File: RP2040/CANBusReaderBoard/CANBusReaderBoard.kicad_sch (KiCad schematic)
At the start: 13 parts, among them J0 RJ45, J1 RJ45, J2 RJ45, J3 RJ45, U1 MCP2515-xSO, U1 RP2040, Y1 Crystal

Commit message: Components all added, need to figure out RP2040 Powering and supplemental components.
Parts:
- removed U1: MCP2515-xSO, Package_SO:SOIC-18W_7.5x11.6mm_P1.27mm, symbol Interface_CAN_LIN:MCP2515-xSO
- removed Y1: Crystal, symbol Device:Crystal
- added C? (x2): 15 pF, Capacitor_THT:C_Axial_L3.8mm_D2.6mm_P7.50mm_Horizontal, symbol Device:C
- added CONTROLLER_1: MCP2515, MCP2515:MCP2515-E&slash_P, symbol Interface_CAN_LIN:MCP2515-xSO
- added J?: Terminate CAN, TerminalBlock_Phoenix:TerminalBlock_Phoenix_MKDS-3-2-5.08_1x02_P5.08mm_Horizontal, symbol Connector_Generic:Conn_01x02
- added R?: 120, Resistor_THT:R_Axial_DIN0204_L3.6mm_D1.6mm_P5.08mm_Horizontal, symbol Device:R_US
- added R?: 10K, Resistor_THT:R_Axial_DIN0204_L3.6mm_D1.6mm_P5.08mm_Horizontal, symbol Device:R_US
- added SW?: SW_DIP_x01, symbol Switch:SW_DIP_x01
- added TRANSCEIVER_1: MCP2562FD, MCP2562FD:MCP2562FD-H&slash_P, symbol MCP2562FD:MCP2562FD-H/P
- added Y?: Crystal 20Mhz, symbol Device:Crystal
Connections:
- net GND: now also C?.1, C?.1, CONTROLLER_1.9 (VSS), TRANSCEIVER_1.3 (VDD)
- net MISO: now also CONTROLLER_1.15 (SO)
- net MOSI: now also CONTROLLER_1.14 (SI)
- new net: R?.1, SW?.1
- new net: C?.2, CONTROLLER_1.8 (OSC1), Y?.1
- new net: C?.2, CONTROLLER_1.7 (OSC2), Y?.2
- new net: CONTROLLER_1.17 (~{RESET}), R?.1
- new net +3V3: CONTROLLER_1.18 (VDD), TRANSCEIVER_1.2 (VSS)
- new net CANH: J?.1 (Pin_1), SW?.2, TRANSCEIVER_1.7 (CANH)
- new net CANL: J?.2 (Pin_2), R?.2, TRANSCEIVER_1.6 (CANL)
- new net CS0: CONTROLLER_1.13 (SCK)
- new net RX: CONTROLLER_1.2 (RXCAN), TRANSCEIVER_1.4 (RXD)
- new net SPICLK: CONTROLLER_1.16 (~{CS})
- new net TX: CONTROLLER_1.1 (TXCAN), TRANSCEIVER_1.1 (TXD)

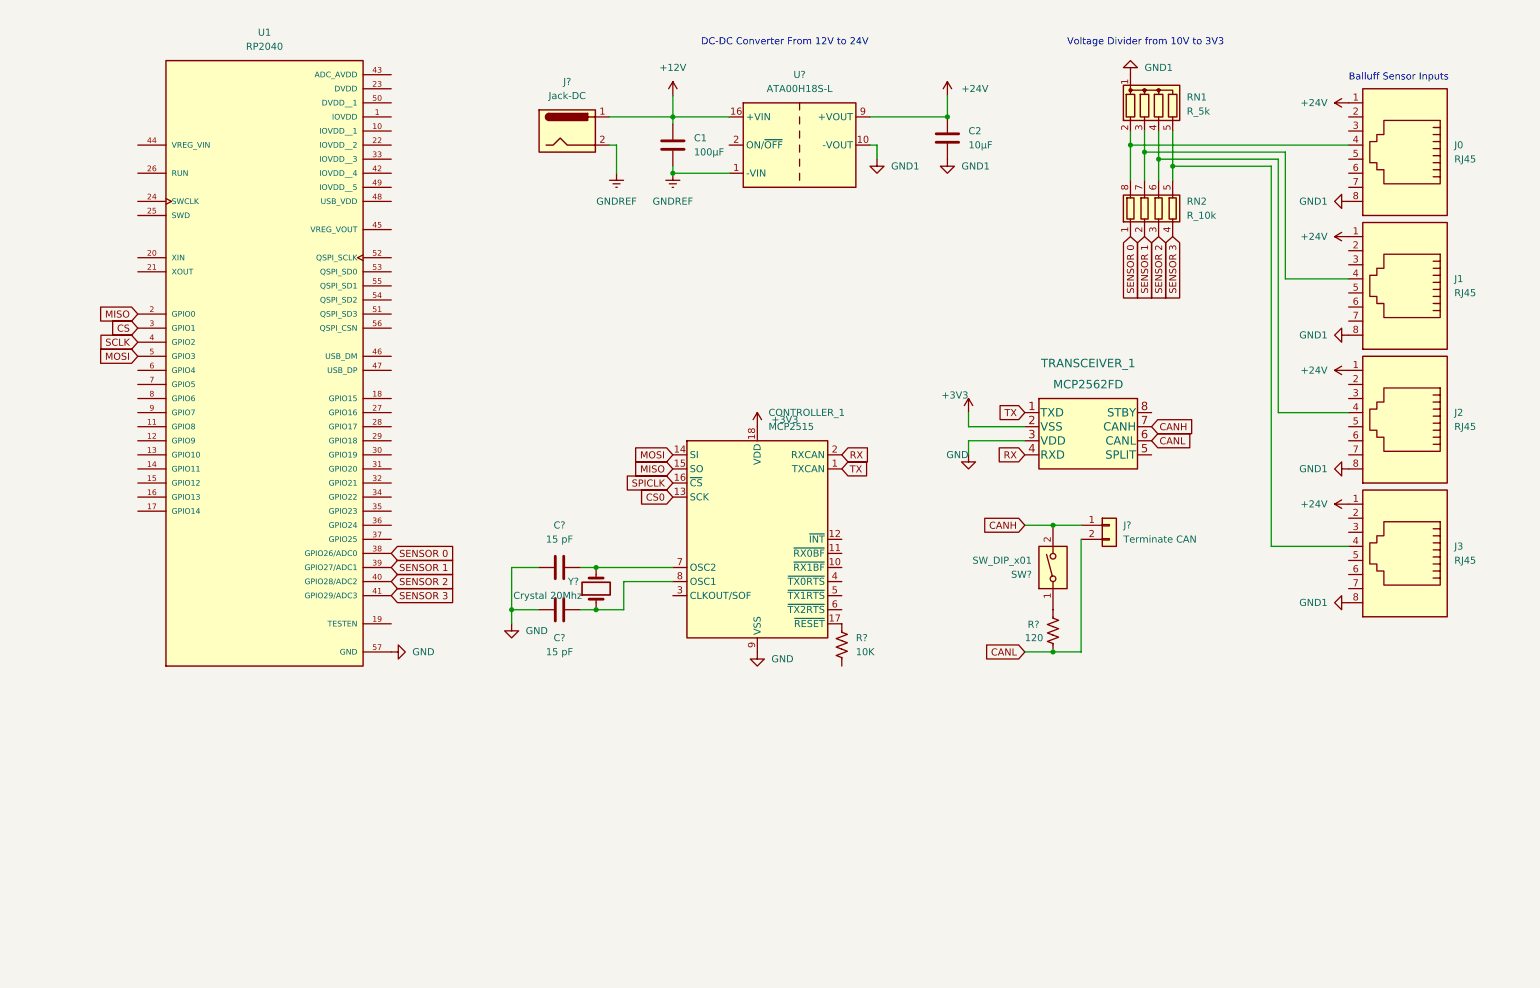
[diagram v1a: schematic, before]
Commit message: voltage regultor to 3.3v
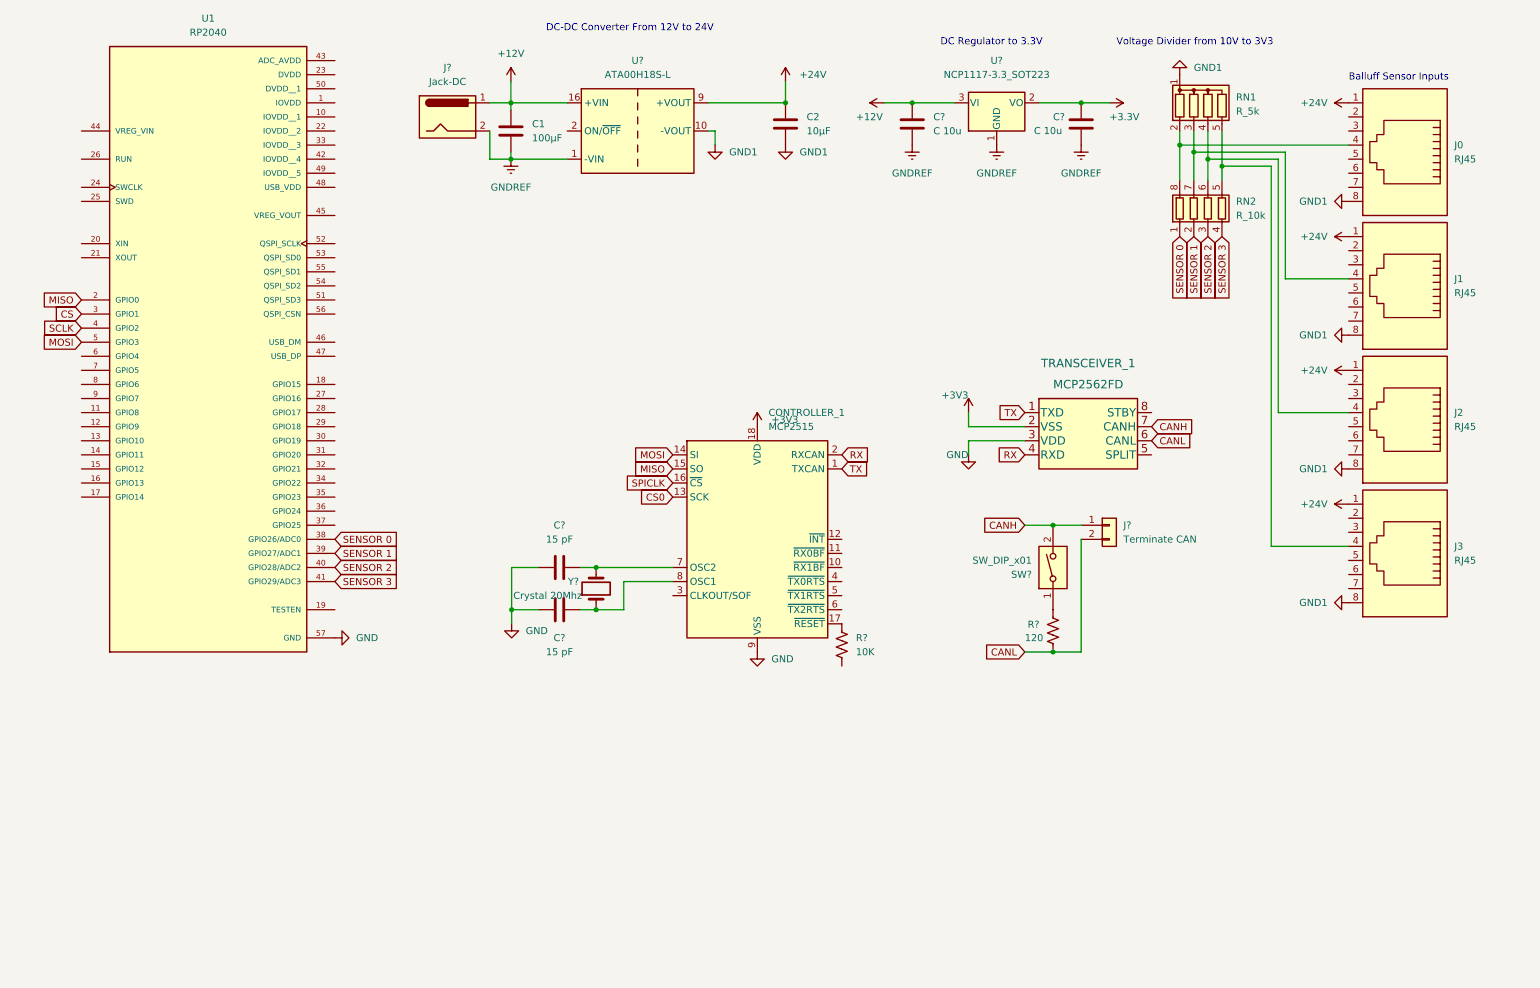
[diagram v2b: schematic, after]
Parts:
- added C? (x2): C 10u, symbol Device:C
- added U?: NCP1117-3.3_SOT223, Package_TO_SOT_SMD:SOT-223-3_TabPin2, symbol Regulator_Linear:NCP1117-3.3_SOT223
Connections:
- net +12V: now also C?.1, U?.3 (VI)
- net GNDREF: now also C?.2, C?.2, U?.1 (GND)
- new net +3.3V: C?.1, U?.2 (VO)
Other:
- note added: "DC Regulator to 3.3V"
- moved on the sheet: C1, C2, J?, RN1, RN2, U1, U?

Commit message: Working on status leds now
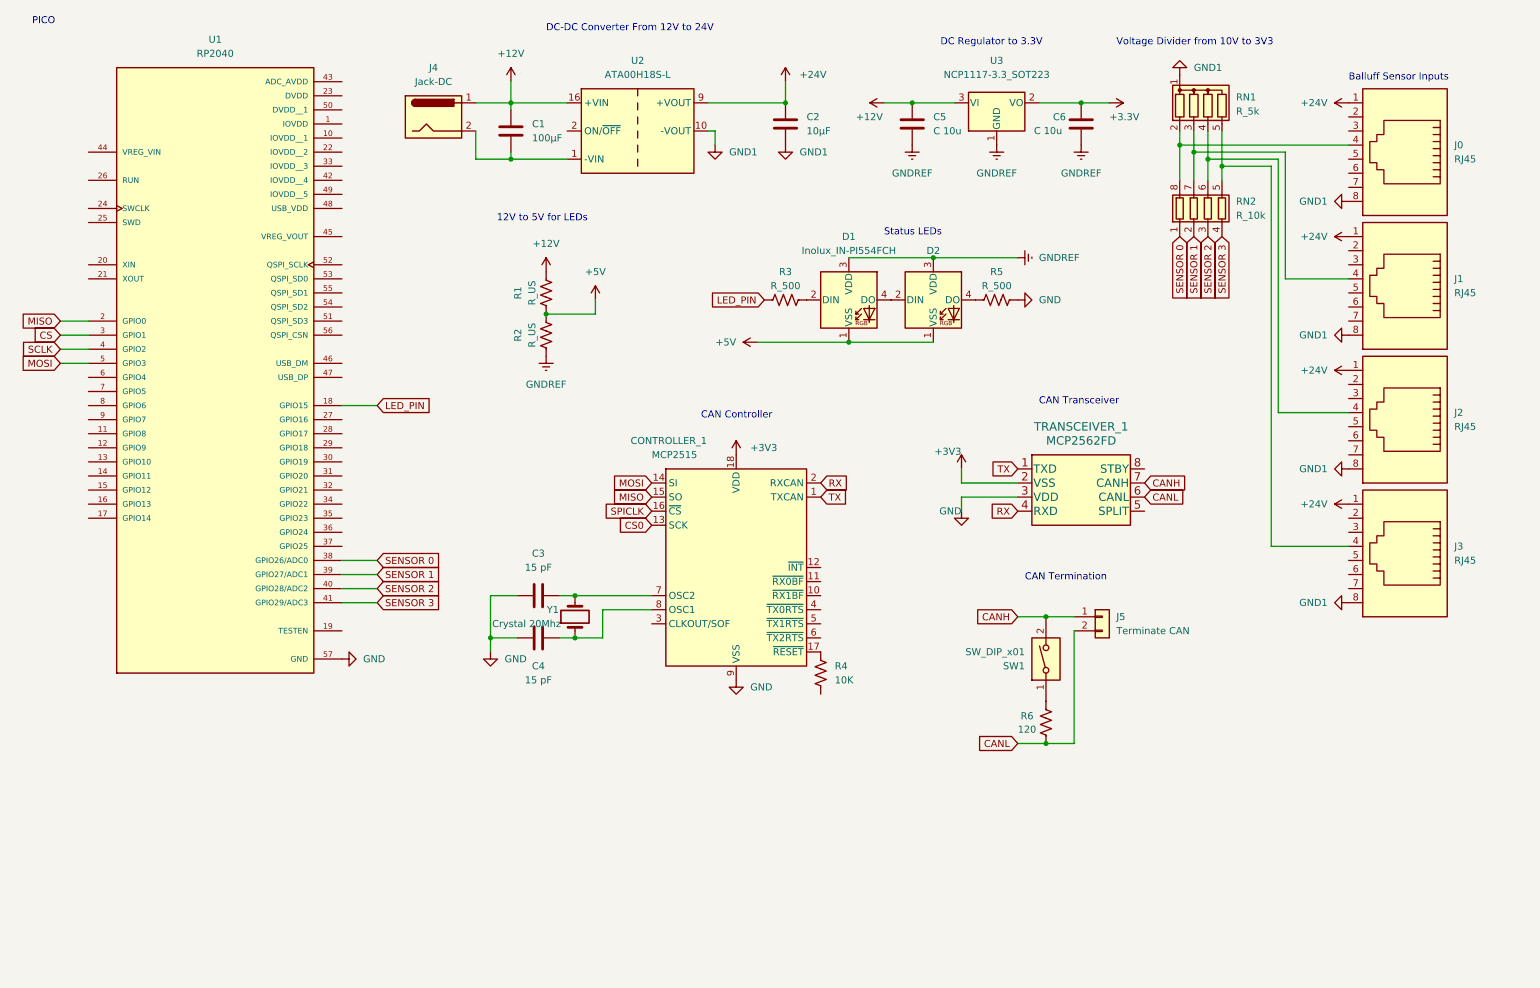
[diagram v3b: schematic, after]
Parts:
- added D1, D2: Inolux_IN-PI554FCH, LED_SMD:LED_Inolux_IN-PI554FCH_PLCC4_5.0x5.0mm_P3.2mm, symbol LED:Inolux_IN-PI554FCH
- added R1, R2: R_US, symbol Device:R_US
- added R3, R5: R_500, symbol Device:R_US
- gave numbers to parts that had none: 12
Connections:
- net +12V: now also R1.2
- net GND: now also R5.2
- net GNDREF: now also D1.3 (VDD), D2.3 (VDD), R2.1; no longer C1.2, J4.2, U2.1 (-VIN)
- net LED_PIN: now reaches U1.18 (GPIO15)
- net LED_PIN: now also R3.1
- new net: D1.4 (DO), D2.2 (DIN)
- new net: D2.4 (DO), R5.1
- new net: C1.2, J4.2, U2.1 (-VIN)
- new net: D1.2 (DIN), R3.2
- new net +5V: D1.1 (VSS), D2.1 (VSS), R1.1, R2.2
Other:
- note added: "12V to 5V for LEDs"
- note added: "CAN Controller"
- note added: "CAN Termination"
- note added: "CAN Transceiver"
- note added: "PICO"
- note added: "Status LEDs"
- moved on the sheet: C3, C4, CONTROLLER_1, J4, J5, R4, R6, SW1, TRANSCEIVER_1, U1, Y1

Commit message: cahnged to pico from rp2040
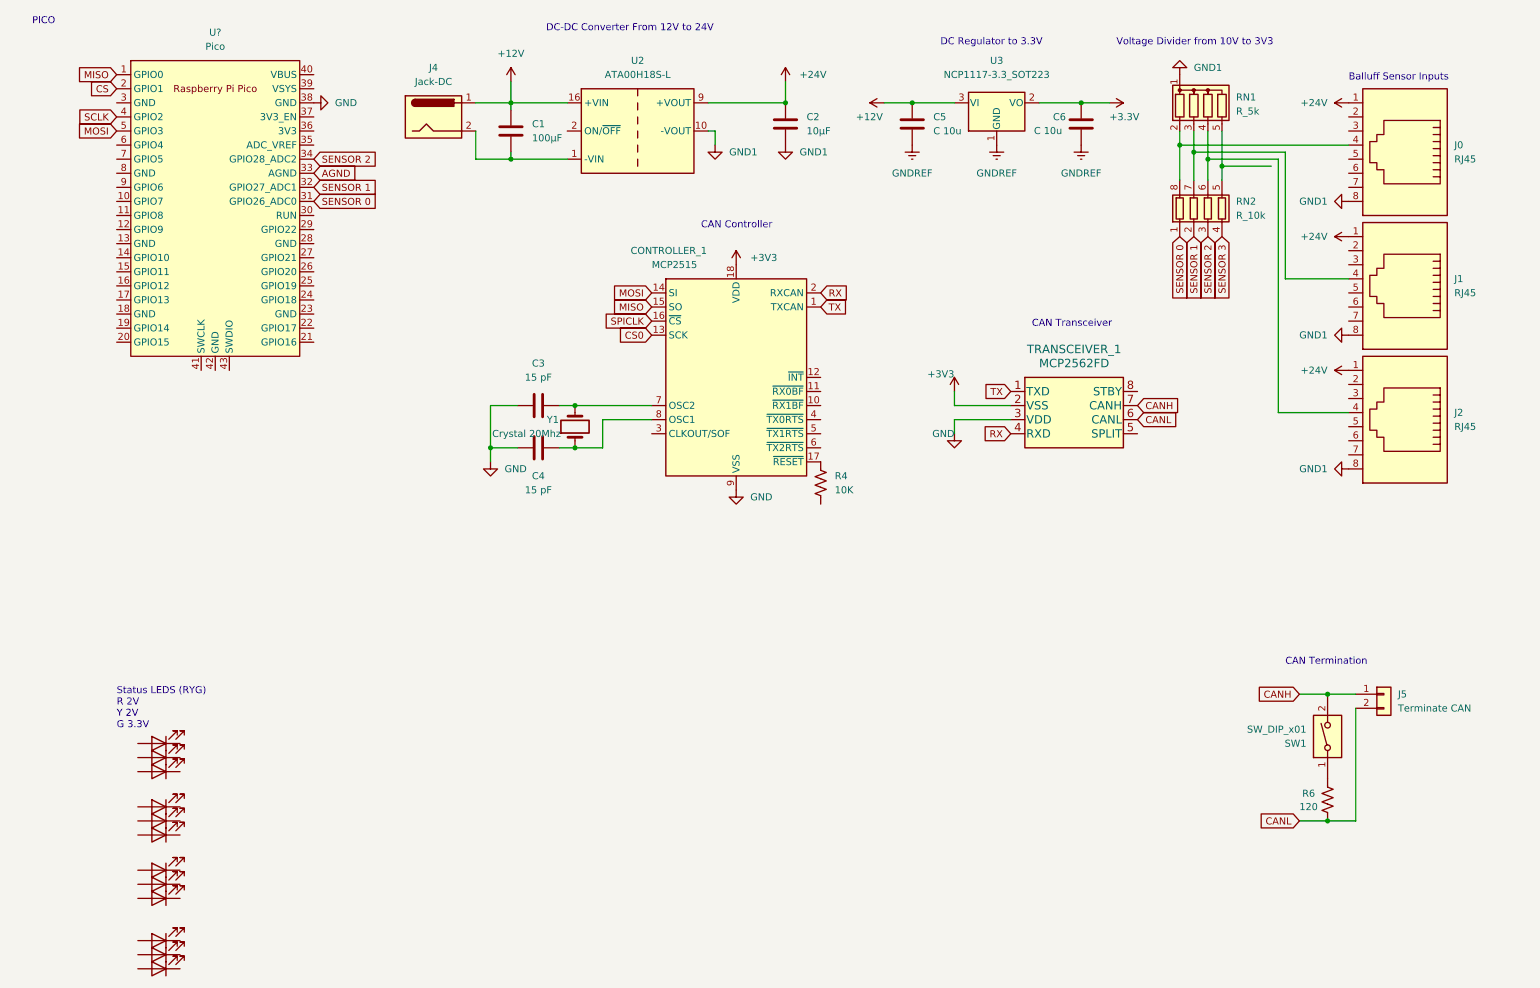
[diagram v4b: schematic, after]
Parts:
- removed D1, D2: Inolux_IN-PI554FCH, LED_SMD:LED_Inolux_IN-PI554FCH_PLCC4_5.0x5.0mm_P3.2mm, symbol LED:Inolux_IN-PI554FCH
- removed J3: RJ45, symbol Connector:RJ45
- removed R1, R2: R_US, symbol Device:R_US
- removed R3, R5: R_500, symbol Device:R_US
- removed U1: RP2040, RP2040:RP2040, symbol RP2040:RP2040
- added D? (x12): LED, symbol Device:LED
- added U?: Pico, RPi_Pico:RPi_Pico_SMD_TH, symbol MCU_RaspberryPi_and_Boards:Pico
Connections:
- net CS: now also U?.2 (GPIO1)
- net GND: now also U?.38 (GND)
- net MISO: now also U?.1 (GPIO0)
- net MOSI: now also U?.5 (GPIO3)
- net SCLK: now also U?.4 (GPIO2)
- net SENSOR 0: now also U?.31 (GPIO26_ADC0)
- net SENSOR 1: now also U?.32 (GPIO27_ADC1)
- net SENSOR 2: now also U?.34 (GPIO28_ADC2)
- new net AGND: U?.33 (AGND)
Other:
- note added: "Status LEDS (RYG) R 2V Y 2V G 3.3V"
- note removed: "12V to 5V for LEDs"
- note removed: "Status LEDs"
- moved on the sheet: C3, C4, CONTROLLER_1, J5, R4, R6, SW1, TRANSCEIVER_1, Y1

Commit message: .
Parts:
- removed CONTROLLER_1: MCP2515, MCP2515:MCP2515-E&slash_P, symbol Interface_CAN_LIN:MCP2515-xSO
- removed D? (x12): LED, symbol Device:LED
- removed R4: 10K, Resistor_THT:R_Axial_DIN0204_L3.6mm_D1.6mm_P5.08mm_Horizontal, symbol Device:R_US
- removed RN1: R_5k, Resistor_THT:R_Array_SIP5, symbol Device:R_Network04
- removed RN2: R_10k, symbol Device:R_Pack04
- removed TRANSCEIVER_1: MCP2562FD, MCP2562FD:MCP2562FD-H&slash_P, symbol MCP2562FD:MCP2562FD-H/P
- removed U3: NCP1117-3.3_SOT223, Package_TO_SOT_SMD:SOT-223-3_TabPin2, symbol Regulator_Linear:NCP1117-3.3_SOT223
- added D? (x5): Inolux_IN-PI554FCH, LED_SMD:LED_Inolux_IN-PI554FCH_PLCC4_5.0x5.0mm_P3.2mm, symbol LED:Inolux_IN-PI554FCH
- added J?: Conn_01x10_Female, symbol Connector:Conn_01x10_Female
- added R1: 10K, Resistor_THT:R_Axial_DIN0207_L6.3mm_D2.5mm_P10.16mm_Horizontal, symbol Device:R_US
- added R2, R3, R4, R5, R7, R8: 100, Resistor_THT:R_Axial_DIN0207_L6.3mm_D2.5mm_P10.16mm_Horizontal, symbol Device:R
- added R? (x4): 500, symbol Device:R
- added U3: MCP2515-E/P, MCP2515-EP:MCP2515-E&slash_P, symbol MCP_2515:MCP2515-E{brace}slash}P
- added U4: L78L05_SOT89, Package_TO_SOT_SMD:SOT-89-3, symbol Regulator_Linear:L78L05_SOT89
- added U5: MCP2562-E-P, Package_DIP:DIP-8_W7.62mm, symbol Interface_CAN_LIN:MCP2562-E-P
- C1, C2, C5, C6: footprint (none) -> Capacitor_THT:C_Axial_L3.8mm_D2.6mm_P7.50mm_Horizontal
- J0, J1, J2: footprint (none) -> Connector_RJ:RJ45_OST_PJ012-8P8CX_Vertical
- J4: footprint (none) -> Connector_BarrelJack:BarrelJack_SwitchcraftConxall_RAPC10U_Horizontal
- R6: footprint Resistor_THT:R_Axial_DIN0204_L3.6mm_D1.6mm_P5.08mm_Horizontal -> Resistor_THT:R_Axial_DIN0207_L6.3mm_D2.5mm_P10.16mm_Horizontal
- SW1: footprint (none) -> Button_Switch_THT:SW_DIP_SPSTx01_Slide_6.7x4.1mm_W7.62mm_P2.54mm_LowProfile
- U1: renamed from U?; footprint RPi_Pico:RPi_Pico_SMD_TH -> MCU_RaspberryPi_and_Boards:RPi_Pico_StandOffs
- Y1: footprint (none) -> Crystal:Crystal_HC33-U_Vertical
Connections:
- net +3.3V is gone; now on net +5V: C6.1
- net +12V: now also U4.3 (IN)
- net +3V3: now also U1.37 (3V3_EN), R1.1, U3.9 (VSS), U5.2 (VSS)
- net CANH: now also U5.7 (CANH)
- net CANL: now also U5.6 (CANL)
- net CS0: now also U3.16 (*CS)
- net GND: now also D?.1 (VSS), D?.1 (VSS), D?.1 (VSS), D?.1 (VSS), D?.1 (VSS), R?.2, R?.2, U3.18 (VDD), U5.3 (VDD)
- net GND1: now also R2.1, R4.1, R7.1
- net GNDREF: now also U4.2 (GND)
- net MISO: now also U3.15 (SO)
- net MOSI: now also U3.14 (SI)
- net RX: now also U3.2 (RXCAN), U5.4 (RXD)
- net SENSOR 0: now also R3.2
- net SENSOR 1: now also R5.2
- net SENSOR 2: now also R8.2
- net SPICLK: now also U3.13 (SCK)
- net TX: now also U3.1 (TXCAN), U5.1 (TXD)
- net at J2.4: now also R7.2, R8.1
- net at J0.4: now also R2.2, R3.1
- net at C4.2, Y1.1: now also U3.8 (OSC1)
- net at C3.2, Y1.2: now also U3.7 (OSC2)
- net at J1.4: now also R4.2, R5.1
- net at U1.10 (GPIO7): now also J?.3 (Pin_3)
- net at U1.11 (GPIO8): now also J?.4 (Pin_4)
- net at U1.12 (GPIO9): now also J?.5 (Pin_5)
- net at U1.13 (GND): now also J?.6 (Pin_6)
- net at U1.14 (GPIO10): now also J?.7 (Pin_7)
- net at U1.15 (GPIO11): now also J?.8 (Pin_8)
- net at U1.16 (GPIO12): now also J?.9 (Pin_9)
- net at U1.17 (GPIO13): now also J?.10 (Pin_10)
- net LED1: now reaches U1.26 (GPIO20)
- net LED1: now also R?.1
- net LED2: now reaches U1.27 (GPIO21)
- net LED2: now also R?.1
- net +5V: now reaches U1.39 (VSYS)
- net +5V: now also D?.3 (VDD), D?.3 (VDD), D?.3 (VDD), D?.3 (VDD), D?.3 (VDD), U4.1 (OUT)
- net at U1.8 (GND): now also J?.1 (Pin_1)
- net at U1.9 (GPIO6): now also J?.2 (Pin_2)
- new net: D?.2 (DIN), R?.2 (x2)
- new net: D?.2 (DIN), D?.4 (DO) (x3)
- new net: D?.4 (DO), R?.1 (x2)
- new net: R1.2, U3.17 (*RESET)
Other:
- note added: "CAN LEDs"
- note added: "Sensor LEDs"
- note removed: "Status LEDS (RYG) R 2V Y 2V G 3.3V"
- moved on the sheet: C3, C4, J5, R6, SW1, Y1

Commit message: ready for wiring
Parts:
- removed J0, J1, J2: RJ45, Connector_RJ:RJ45_OST_PJ012-8P8CX_Vertical, symbol Connector:RJ45
- added J2: 3xRJ45V, 3xRJ45V:3xRJ45V, symbol 3xRJ45V:3xRJ45V
- J1: renamed from J?; footprint (none) -> Connector_PinHeader_2.54mm:PinHeader_1x10_P2.54mm_Vertical
- R10, R11, R12, R9: renamed from R?; footprint (none) -> Resistor_THT:R_Axial_DIN0207_L6.3mm_D2.5mm_P10.16mm_Horizontal
- gave numbers to parts that had none: 5
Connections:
- net +24V: now also J2.A1, J2.B1, J2.C1
- net GND1: now also J2.A8, J2.B8, J2.C8
- net SENSOR 2 (24V): now reaches R7.2, R8.1
- net SENSOR 2 (24V): now also J2.C5
- net SENSOR 0 (24V): now reaches R2.2, R3.1
- net SENSOR 0 (24V): now also J2.A5
- net SENSOR 1 (24V): now reaches R4.2, R5.1
- net SENSOR 1 (24V): now also J2.B5
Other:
- moved on the sheet: J5, R6, SW1
